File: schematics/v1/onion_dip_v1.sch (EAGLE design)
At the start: 26 parts

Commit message: added EEPROM, SPI, SMB Diode
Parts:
- added D2: (no value), diode:DIODE-SMB
- added IC2: DS2432P, 1wire:DS2432P
- added R1: (no value), rcl:R-EU_R0805
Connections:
- removed net N$18: SV9.6
- removed net N$19: SV9.8
- removed net N$21: SV9.5
- removed net N$22: SV9.7
- removed net N$23: SV4.4
- removed net N$24: SV4.6
- removed net N$25: SV4.8
- removed net N$26: SV4.3
- removed net N$31: SV4.5
- removed net N$32: SV4.7
- net CSICK: now also SV4.6, SV9.6
- net CSIHSYNC: now also SV4.3, SV9.3
- net CSIPCK: now also SV4.4, SV9.4
- net CSVSYNC: now also SV4.5, SV9.5
- net D2: now also SV4.7
- net D3: now also SV4.8
- net GND: now also IC2P.GND; no longer SV15.1, SV15.2
- net LD2: now also IC2_1W.1W, R1.1
- net N$1: now also D2.A
- net P7: now also SV9.7, SV9.8; no longer SV9.3, SV9.4
- net VCC: now also D2.C, R1.2
- net Y2: now also SV15.1, SV15.2
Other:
- note added: "SPI2_CLK"
- note added: "SPI2_CS0"
- note added: "SPI2_MISO"
- note added: "SPI2_MOSI"

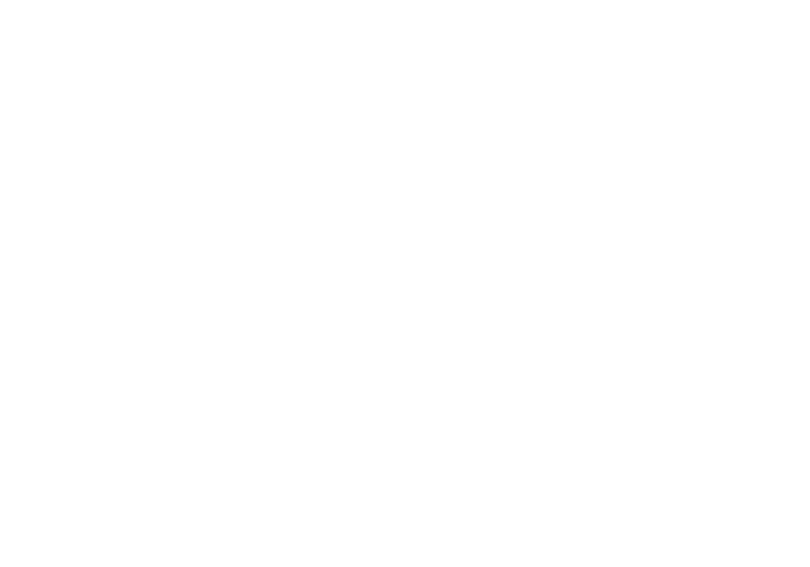
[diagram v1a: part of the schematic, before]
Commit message: added UART header
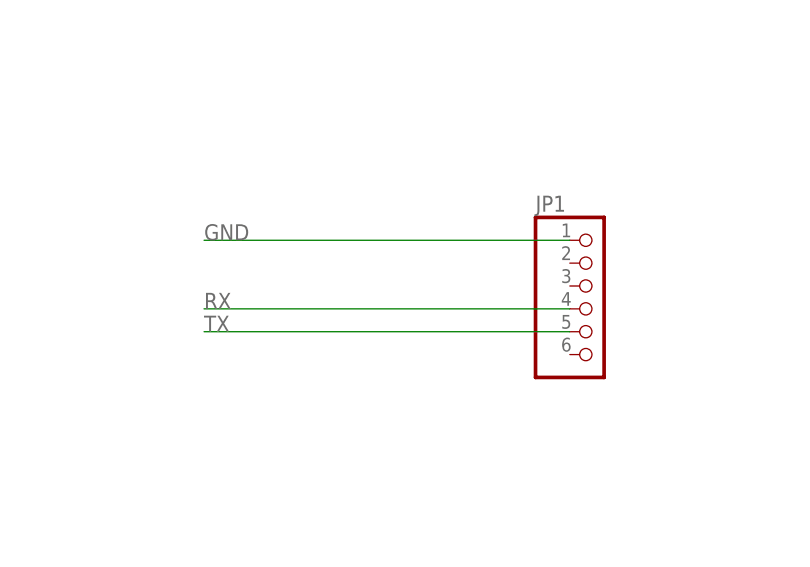
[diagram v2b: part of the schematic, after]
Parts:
- added JP1: (no value), pinhead:PINHD-1X6
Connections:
- net GND: now also JP1.1
- net RX: now also JP1.4
- net TX: now also JP1.5
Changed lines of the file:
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@@
 <part name="P+3" library="supply1" deviceset="VCC" device=""/>
 <part name="D2" library="diode" deviceset="DIODE-" device="SMB"/>
+<part name="JP1" library="pinhead" deviceset="PINHD-1X6" device=""/>
 </parts>
 <sheets>
@@
 </instance>
 <instance part="D2" gate="G$1" x="-53.34" y="88.9" rot="R90"/>
+<instance part="JP1" gate="A" x="266.7" y="86.36"/>
 </instances>
 <busses>
@@
 <wire x1="-17.78" y1="17.78" x2="-17.78" y2="15.24" width="0.1524" layer="91"/>
 </segment>
+<segment>
+<pinref part="JP1" gate="A" pin="1"/>
+<wire x1="223.52" y1="93.98" x2="264.16" y2="93.98" width="0.1524" layer="91"/>
+<label x="223.52" y="93.98" size="1.778" layer="95"/>
+</segment>
 </net>
 <net name="P5" class="0">
@@
 <label x="317.5" y="185.42" size="1.778" layer="95"/>
 </segment>
+<segment>
+<pinref part="JP1" gate="A" pin="4"/>
+<wire x1="223.52" y1="86.36" x2="264.16" y2="86.36" width="0.1524" layer="91"/>
+<label x="223.52" y="86.36" size="1.778" layer="95"/>
+</segment>
 </net>
 <net name="TX" class="0">
@@
 <label x="317.5" y="187.96" size="1.778" layer="95"/>
 </segment>
-</net>
+<segment>
+<pinref part="JP1" gate="A" pin="5"/>
+<wire x1="223.52" y1="83.82" x2="264.16" y2="83.82" width="0.1524" layer="91"/>
+<label x="223.52" y="83.82" size="1.778" layer="95"/>
+</segment>
+</net>

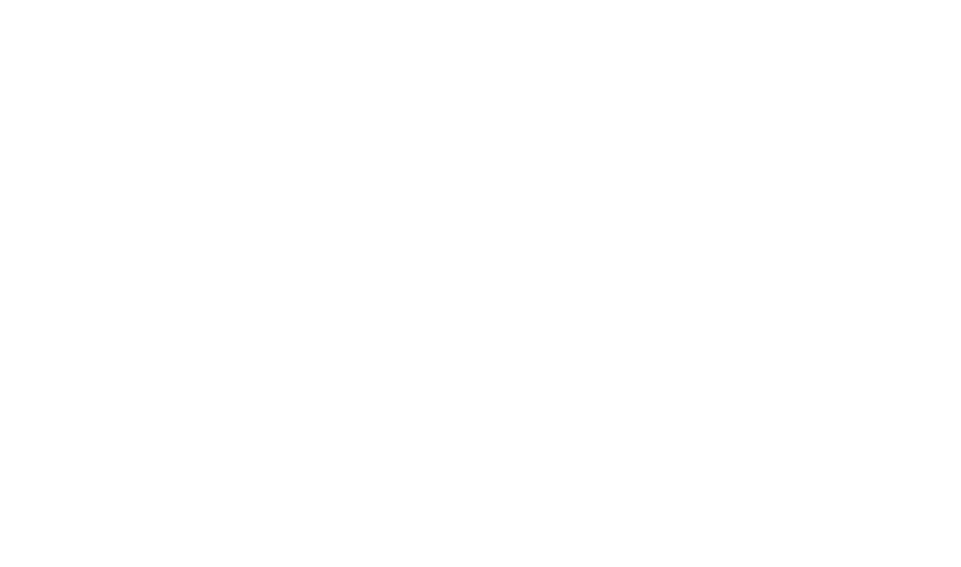
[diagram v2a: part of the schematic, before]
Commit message: new logo
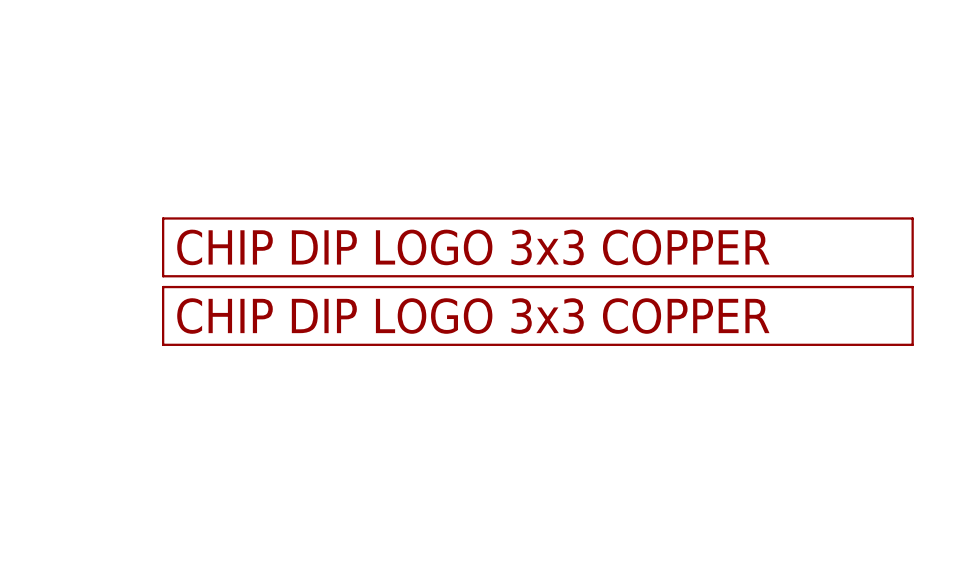
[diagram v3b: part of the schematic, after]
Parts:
- added U$4, U$6: LOGO_3X3_COPPER, logo:LOGO_3X3_COPPER
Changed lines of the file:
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@@
 <part name="D2" library="diode" deviceset="DIODE-" device="SMB"/>
 <part name="JP1" library="pinhead" deviceset="PINHD-1X6" device=""/>
+<part name="U$4" library="logo" deviceset="LOGO_3X3_COPPER" device=""/>
+<part name="U$6" library="logo" deviceset="LOGO_3X3_COPPER" device=""/>
 </parts>
 <sheets>
@@
 <instance part="D2" gate="G$1" x="-53.34" y="88.9" rot="R90"/>
 <instance part="JP1" gate="A" x="266.7" y="86.36"/>
+<instance part="U$4" gate="G$1" x="289.56" y="109.22"/>
+<instance part="U$6" gate="G$1" x="289.56" y="101.6"/>
 </instances>
 <busses>

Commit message: add silkscreen and forum wishes
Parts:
- removed JP1: (no value), pinhead:PINHD-1X6
- removed PAD1, PAD2: WIREPAD3,17/1,3, wirepad:WIREPAD3,17/1,3
- added ASDASD: (no value), pinhead:PINHD-1X6
- added GND, VIN: WIREPAD3,17/1,3, wirepad:WIREPAD3,17/1,3
- added LED1, LED2: (no value), led:LEDCHIP-LED0805
- added R2, R3: 330R, rcl:R-EU_R0805
- added U$5: LOGO_10X10_SILK, logo:LOGO_10X10_SILK
- SV1, SV10, SV11, SV4, SV9: device con-lstb:MA05-2 -> con-lstb_no_frame:MA05-2
- SV12, SV15, SV16, SV6: device con-lstb:MA03-2 -> con-lstb_no_frame:MA03-2
- SV14: device con-lstb:MA06-2 -> con-lstb_no_frame:MA06-2
- SV20, SV21: device con-lstb:MA07-2 -> con-lstb_no_frame:MA07-2
- U$9: value MP1584EN -> MP1584EN_FRAMELESS; device power_supply:MP1584EN -> power_supply:MP1584EN_FRAMELESS
- renumbered PAD3 to IN, PAD4 to N_CLOSE, PAD5 to N_OPEN
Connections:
- removed net N$1: D1.A, D2.A, U$1.COIL0, U$3.D
- new net N$3: LED1.C, R2.1
- new net N$4: LED2.C, R3.1
- new net N4: SV9.7, SV9.8
- new net N5: SV9.10, SV9.9
- new net RELAY_LO: D1.A, D2.A, R7.2, U$1.COIL0, U$3.D
- net GND: now also ASDASD.1, GND.P; no longer JP1.1, PAD2.P, R7.2, SV14.11, SV14.12
- net P0: now also R3.2
- net P3: now also R2.2
- net P7: now also SV14.11, SV14.12; no longer SV9.7, SV9.8
- net RX: now also ASDASD.4; no longer JP1.4
- net TX: now also ASDASD.5; no longer JP1.5
- net VCC: now also LED1.A, LED2.A; no longer SV9.10, SV9.9
- net VIN: now also VIN.P; no longer PAD1.P
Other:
- moved on the sheet: JP3, LED5, R7, SV1, SV10, SV11, SV12, SV14, SV15, SV16, SV20, SV21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

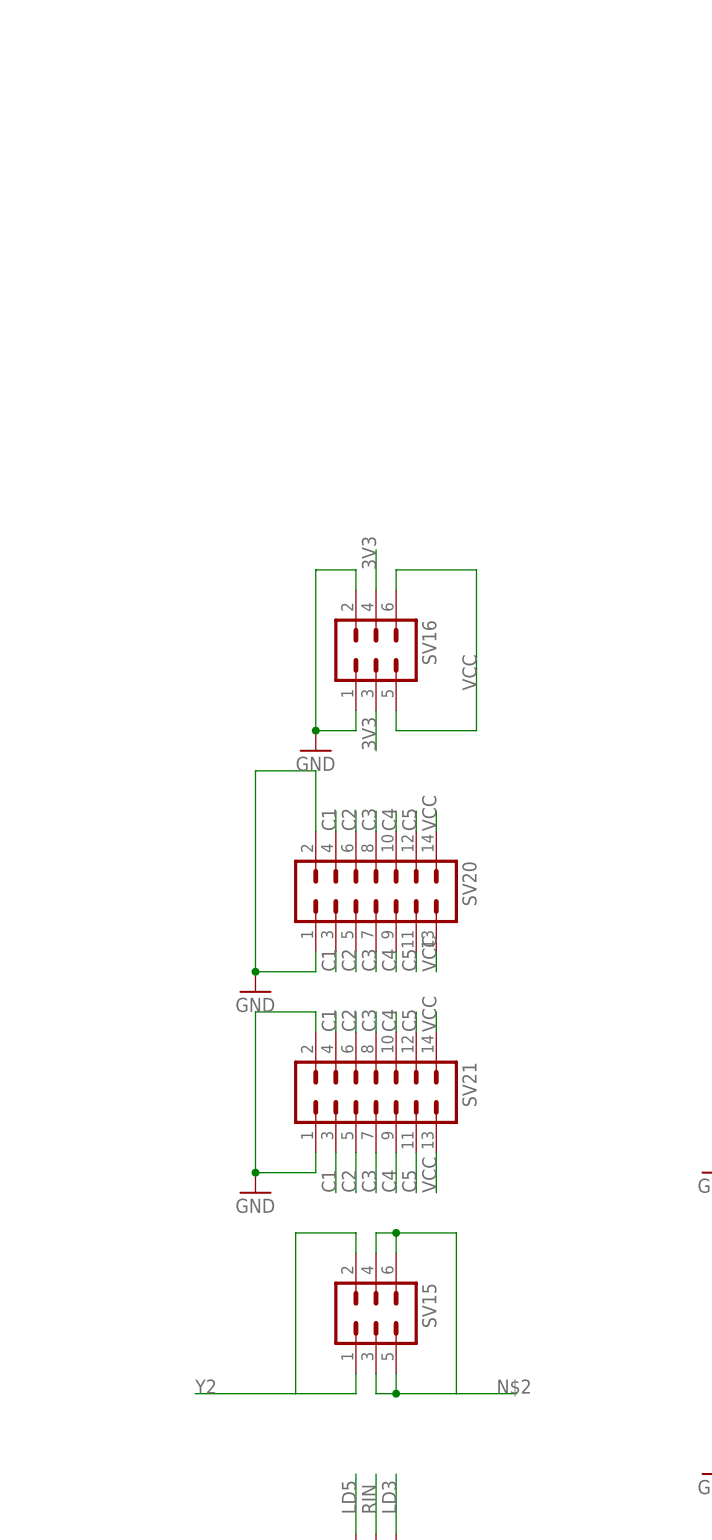
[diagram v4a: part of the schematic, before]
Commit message: added more pins for DIP tinker area
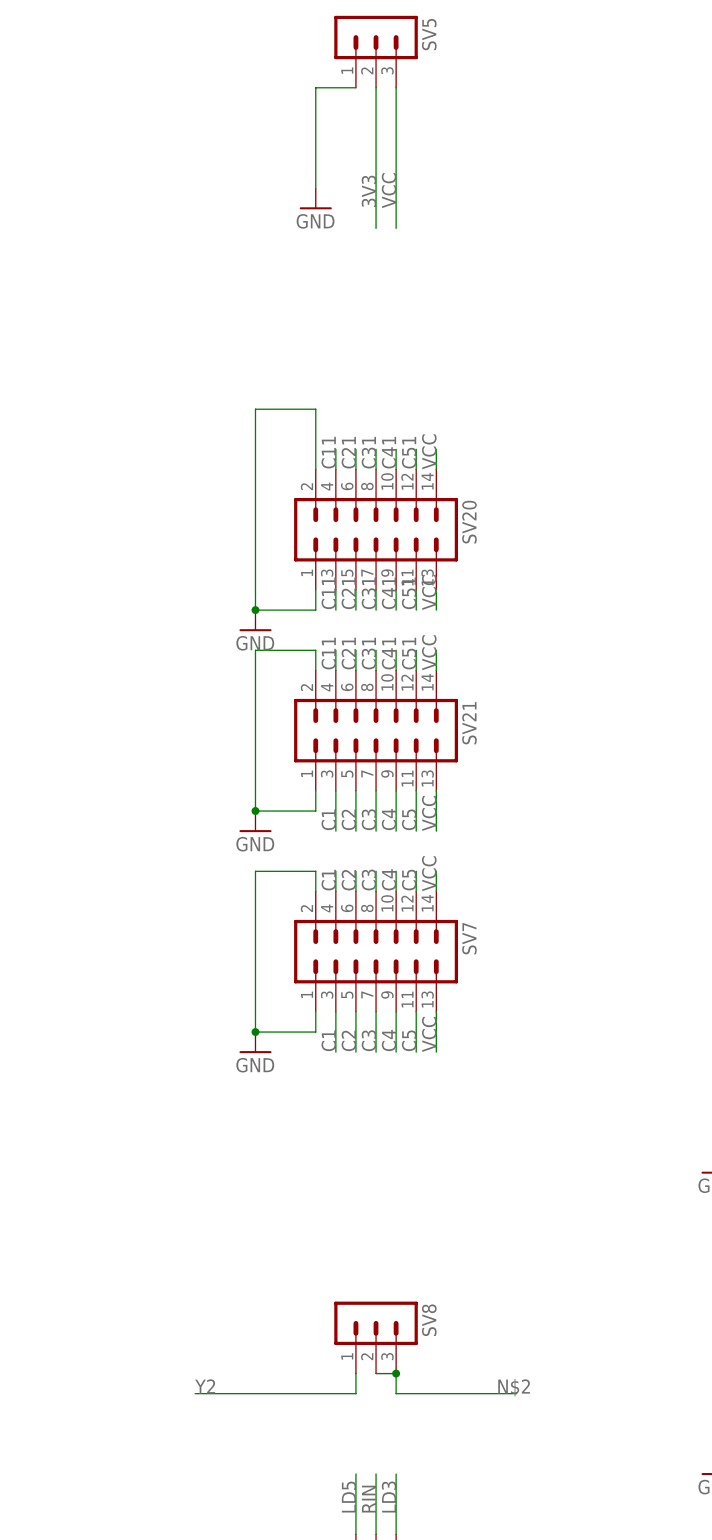
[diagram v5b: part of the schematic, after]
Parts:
- removed SV15, SV16: (no value), con-lstb_no_frame:MA03-2
- added SV5, SV8: (no value), con-lstb_no_frame:MA03-1
- added SV7: (no value), con-lstb_no_frame:MA07-2
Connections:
- new net C11: SV20.3, SV20.4, SV21.4
- new net C21: SV20.5, SV20.6, SV21.6
- new net C31: SV20.7, SV20.8, SV21.8
- new net C41: SV20.10, SV20.9, SV21.10
- new net C51: SV20.11, SV20.12, SV21.12
- net 3V3: now also SV5.2; no longer SV16.3, SV16.4
- net C1: now also SV7.3, SV7.4; no longer SV20.3, SV20.4, SV21.4
- net C2: now also SV7.5, SV7.6; no longer SV20.5, SV20.6, SV21.6
- net C3: now also SV7.7, SV7.8; no longer SV20.7, SV20.8, SV21.8
- net C4: now also SV7.10, SV7.9; no longer SV20.10, SV20.9, SV21.10
- net C5: now also SV7.11, SV7.12; no longer SV20.11, SV20.12, SV21.12
- net GND: now also SV5.1, SV7.1, SV7.2; no longer SV16.1, SV16.2
- net N$2: now also SV8.2, SV8.3; no longer SV15.3, SV15.4, SV15.5, SV15.6
- net VCC: now also SV5.3, SV7.13, SV7.14; no longer SV16.5, SV16.6
- net Y2: now also SV8.1; no longer SV15.1, SV15.2
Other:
- moved on the sheet: SV20, SV21
